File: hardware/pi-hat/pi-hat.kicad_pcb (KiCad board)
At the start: 2 copper layers, 70.6 x 36.6 mm, 33 parts, among them J1 ENC_1, J10 PWR_OUT_B, J11 I2C_OUT_A, J12 BOARDS_RESET, J13 PWR_LED, J14 I2C_OUT_B, J2 ENC_2, J3 BTN_1, J4 BTN_2, J5 BTN_3, J6 Raspberry, J7 PWR_IN, J8 PWR_OUT_PI, J9 PWR_OUT_A, Q1 BC846, Q2 BC846, Q3 BC846, Q4 BSS138, Q5 BSS138, SW1 PWR_SW

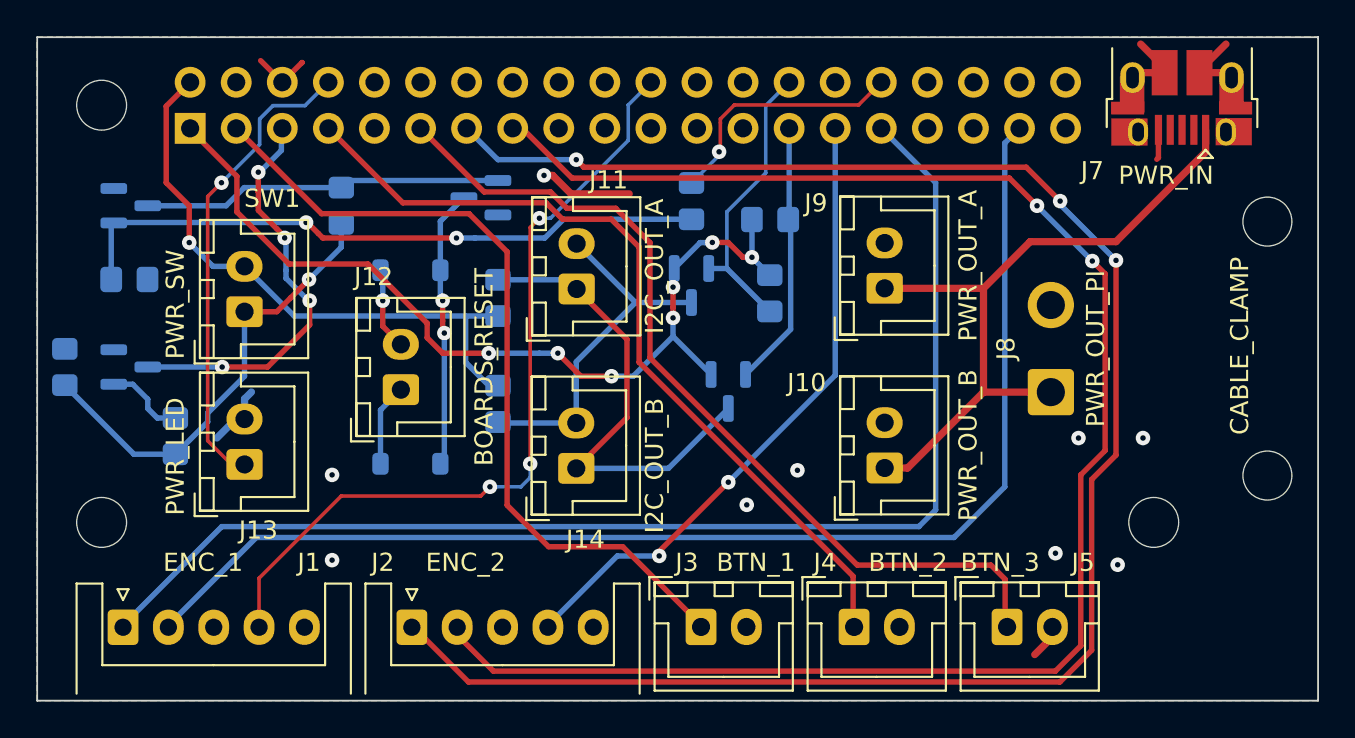
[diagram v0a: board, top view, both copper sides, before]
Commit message: pi-hat: make the rounded-track layout the current PCB
pi-hat.kicad_pcb is now the layout that was actually fabricated
(rounded tracks, ex pihat_smd-rounded-blah); the previous straight-
track layout moves to variants/pi-hat_unrounded with its own project
file. The four solder-mask-bridge DRC exclusions from the rounded
layout's project file were carried over into pi-hat.kicad_pro.
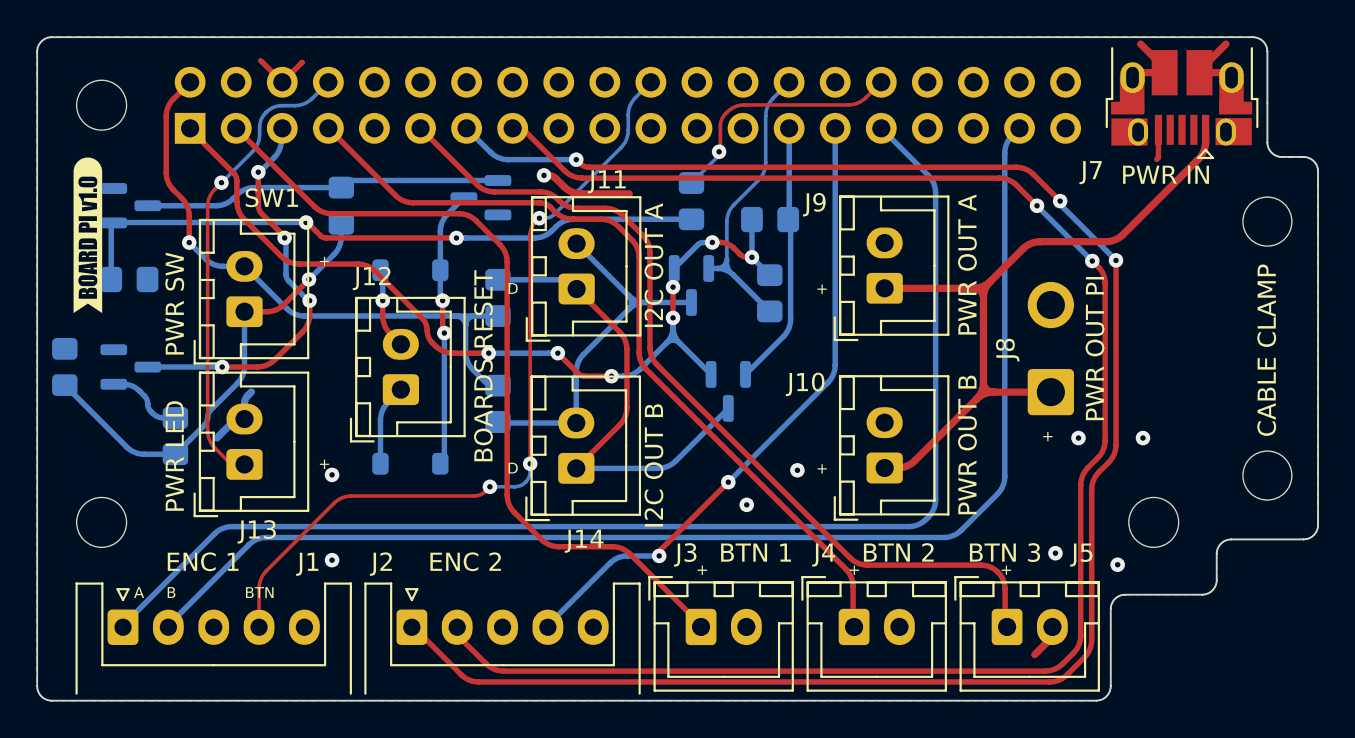
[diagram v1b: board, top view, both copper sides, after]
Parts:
- added REF**: OSHW-Logo2_7.3x6mm_Copper, Symbol:OSHW-Logo2_7.3x6mm_Copper, B.Cu at (122.4, 109.0)
- added kibuzzard-641898A3: G***, kibuzzard-641898A3, F.Cu at (63.8, 102.4)
- added kibuzzard-641898BA: G***, kibuzzard-641898BA, F.Cu at (63.8, 110.7)
- CH1: value CABLE_CLAMP -> CABLE CLAMP
- J1: value ENC_1 -> ENC 1
- J10: value PWR_OUT_B -> PWR OUT B
- J11: value I2C_OUT_A -> I2C OUT A
- J12: value BOARDS_RESET -> BOARDS RESET
- J13: value PWR_LED -> PWR LED
- J14: value I2C_OUT_B -> I2C OUT B
- J2: value ENC_2 -> ENC 2
- J3: value BTN_1 -> BTN 1
- J4: value BTN_2 -> BTN 2
- J5: value BTN_3 -> BTN 3
- J7: value PWR_IN -> PWR IN
- J8: value PWR_OUT_PI -> PWR OUT PI
- J9: value PWR_OUT_A -> PWR OUT A
- SW1: value PWR_SW -> PWR SW
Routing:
- net /EXT_5V: track 38.6 -> 40.9 mm
- net /I2C_CLK_5V: track 20.0 -> 21.2 mm
- net /I2C_CLK: track 16.0 -> 17.0 mm
- net +5V: track 33.5 -> 34.2 mm
- net +3.3V: track 50.3 -> 50.9 mm
- net /BTN_3: track 48.8 -> 48.2 mm
- net /ENC_2_B: track 93.4 -> 92.8 mm
- net /ENC_2_A: track 100.5 -> 100.0 mm
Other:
- outline, holes or cut-outs redrawn
- board text added: "+"
- board text added: "A"
- board text added: "B"
- board text added: "BTN"
- board text added: "D"
- board text added: "I am a banana"
- board text added: "JLCJLCJLCJLC"
- board text added: "KOT_BEHEMOT 2023"
